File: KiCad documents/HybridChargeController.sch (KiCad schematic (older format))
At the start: 90 parts, among them P1 Load, P2 LI_balancer, P3 PV, P4 Extra, P5 LI, P6 LA, Q1 MMBT3904, Q10 MMBT3904, Q11 IPD90P04P4L-04, Q12 STL60P4LLF6, Q13 STL60P4LLF6, Q2 IPD90P04P4L-04, Q3 RQ3E100BNTB, Q4 IPD90P04P4L-04, Q5 RQ3E100BNTB, Q6 MMBT3904, Q7 BSS138, Q8 MMBT3904, Q9 IPD90P04P4L-04, U1 LM358D, U2 bq76920, U3 cd4051, U4 LM358D, U5 LM358D

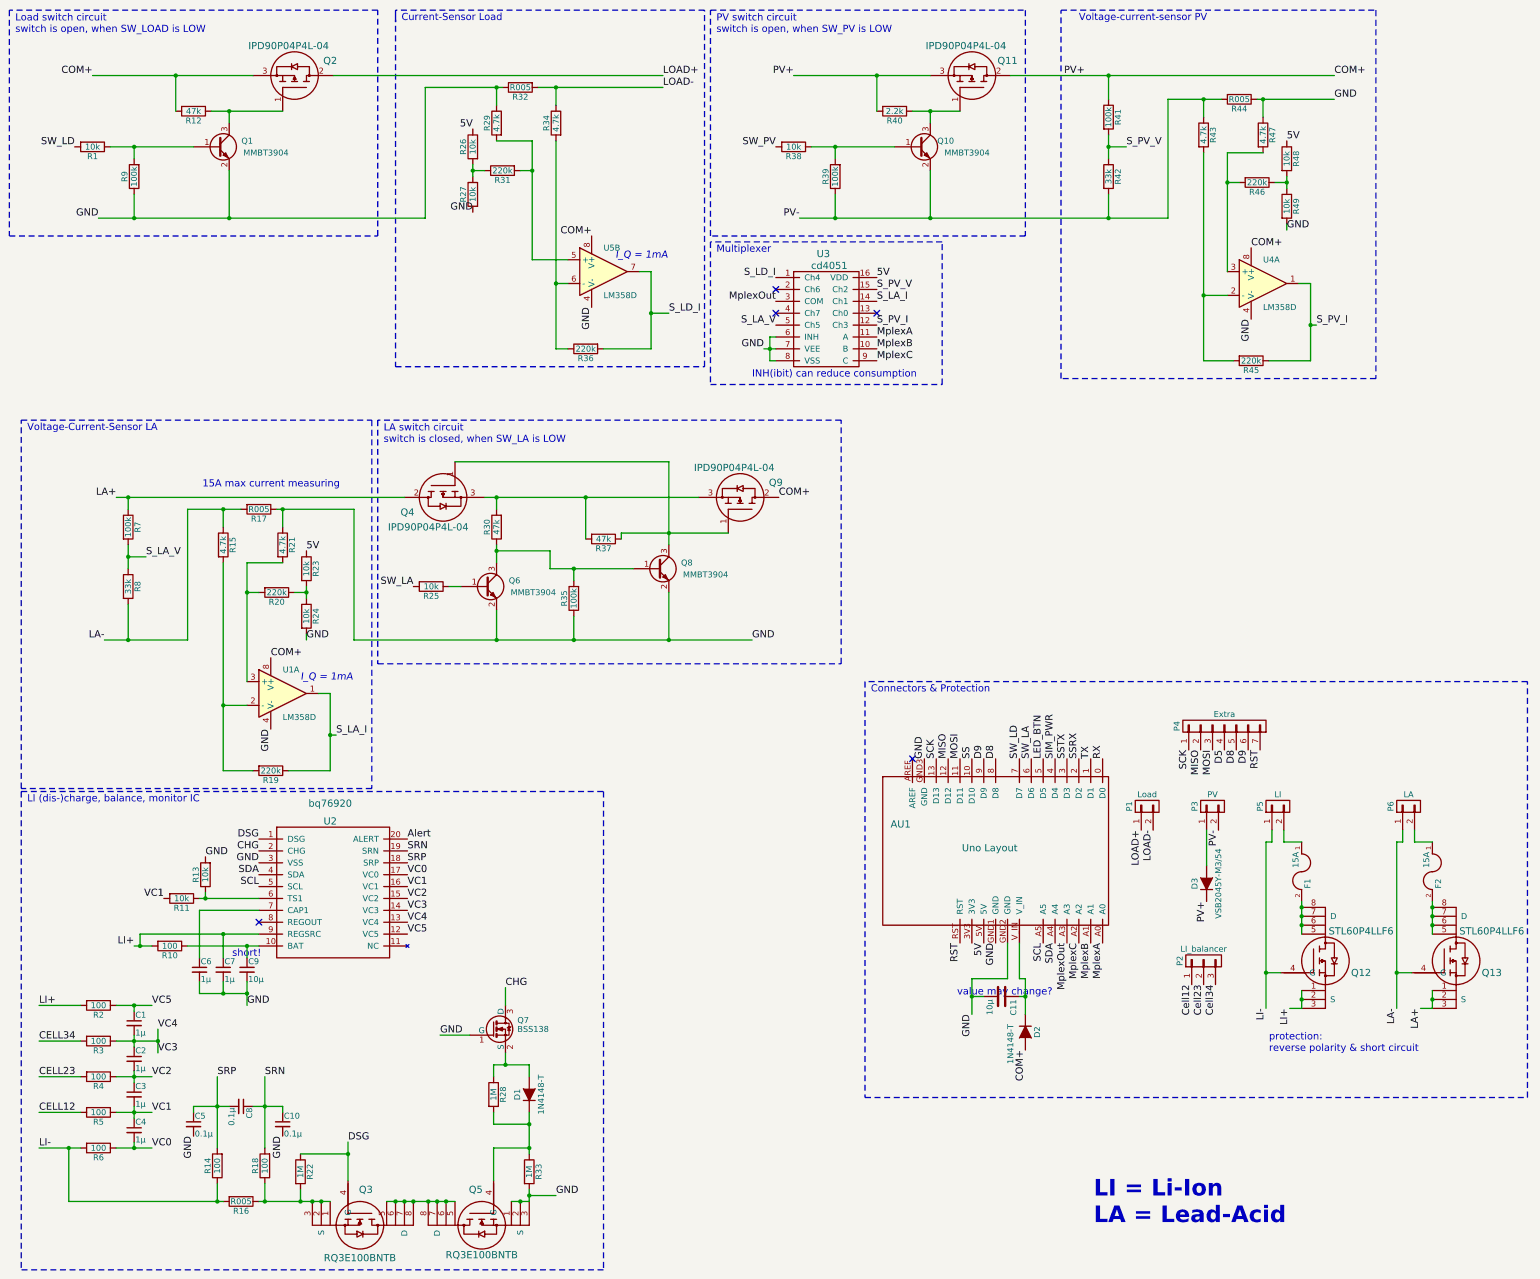
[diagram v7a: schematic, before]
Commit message: noticed low side switching
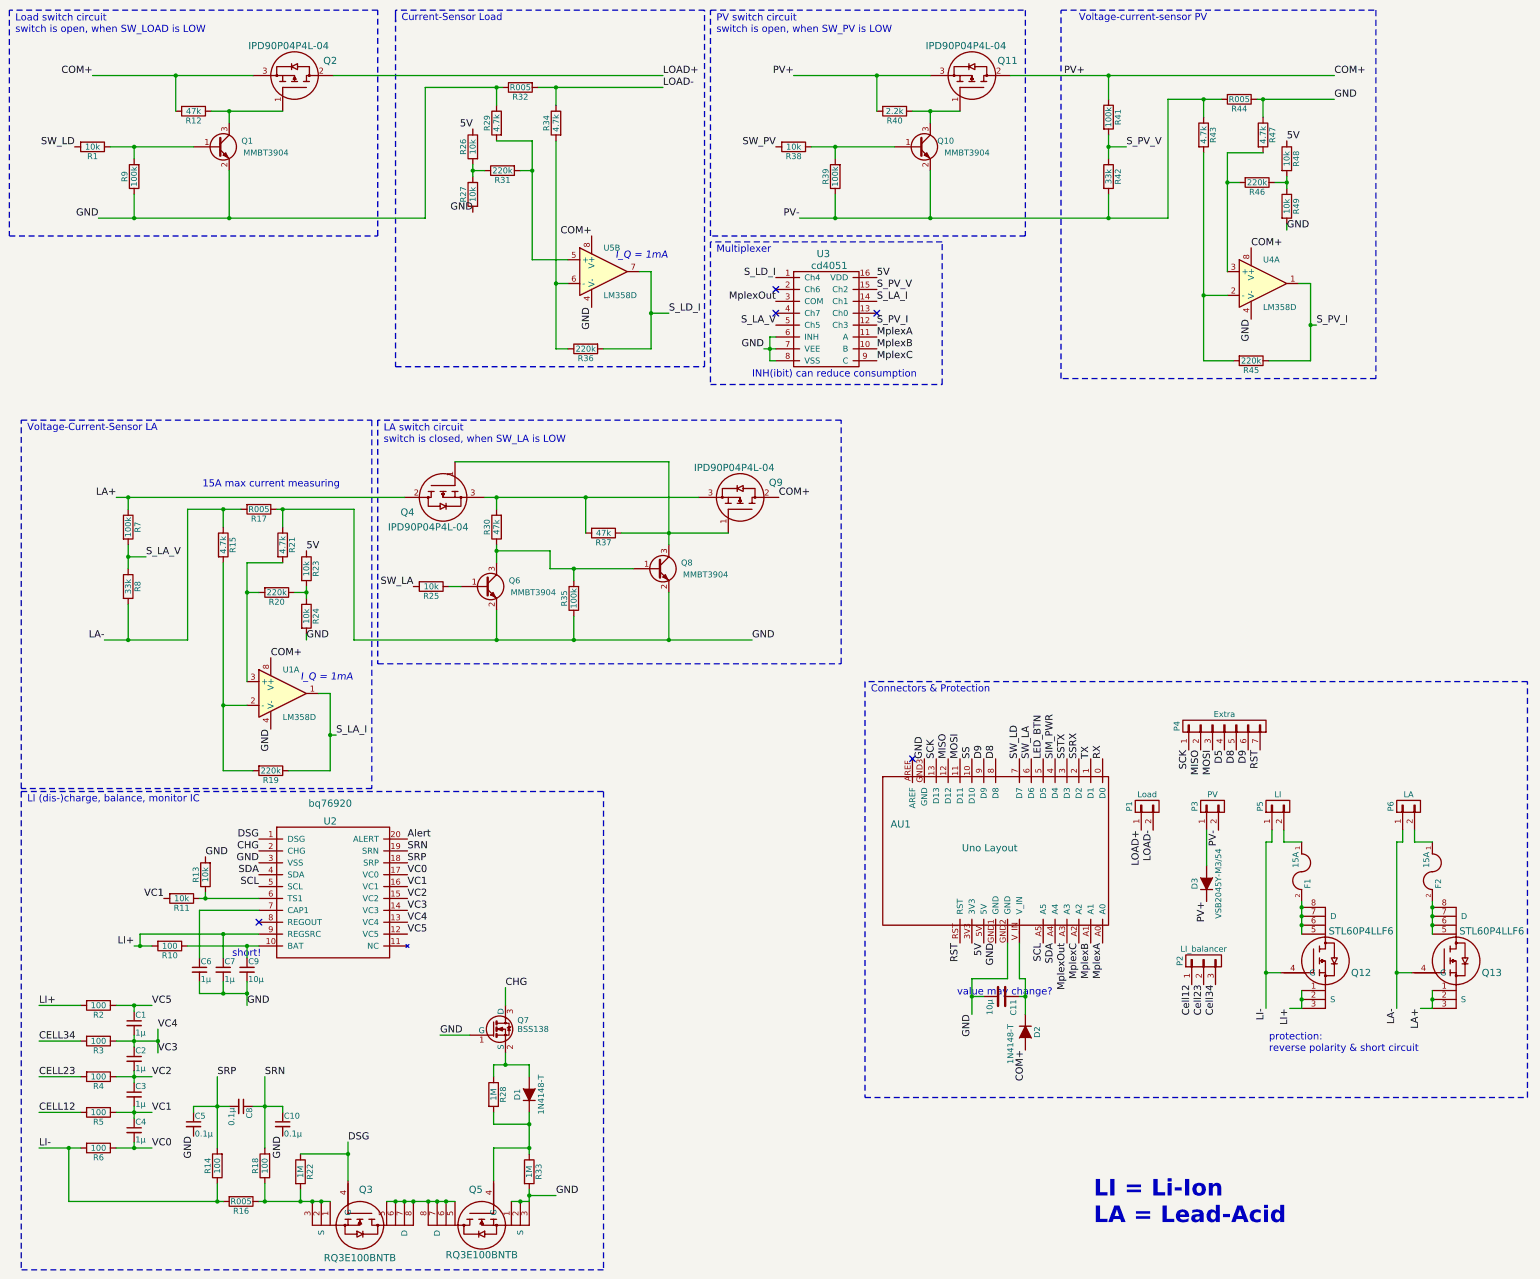
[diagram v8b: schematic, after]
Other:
- moved on the sheet: R37
